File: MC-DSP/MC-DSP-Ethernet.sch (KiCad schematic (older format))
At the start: 29 parts

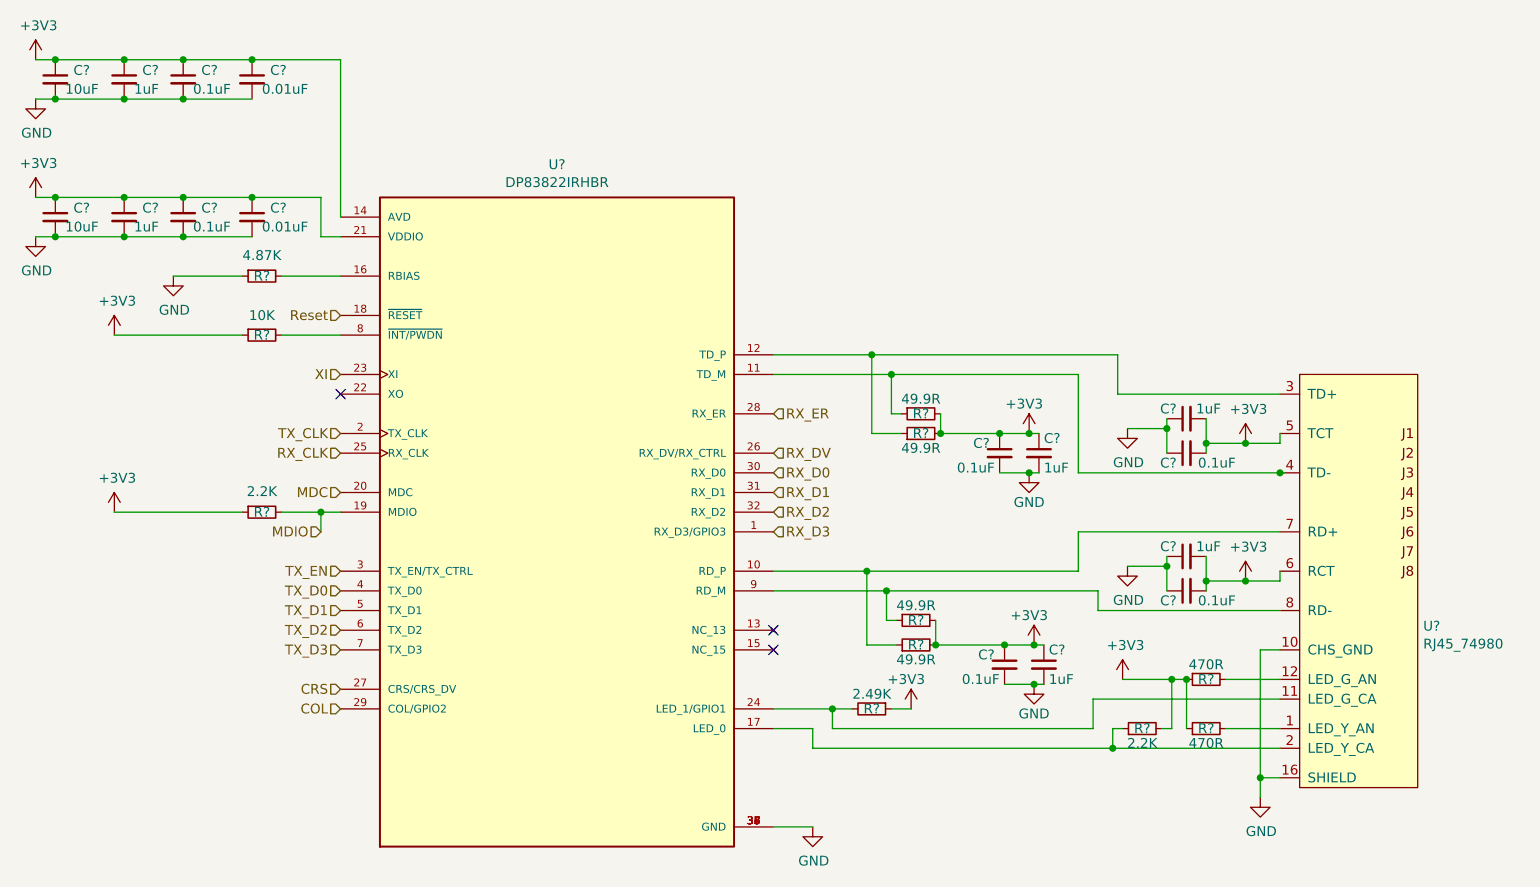
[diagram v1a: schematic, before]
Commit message: All parts labeled, just need to pick passives basically.
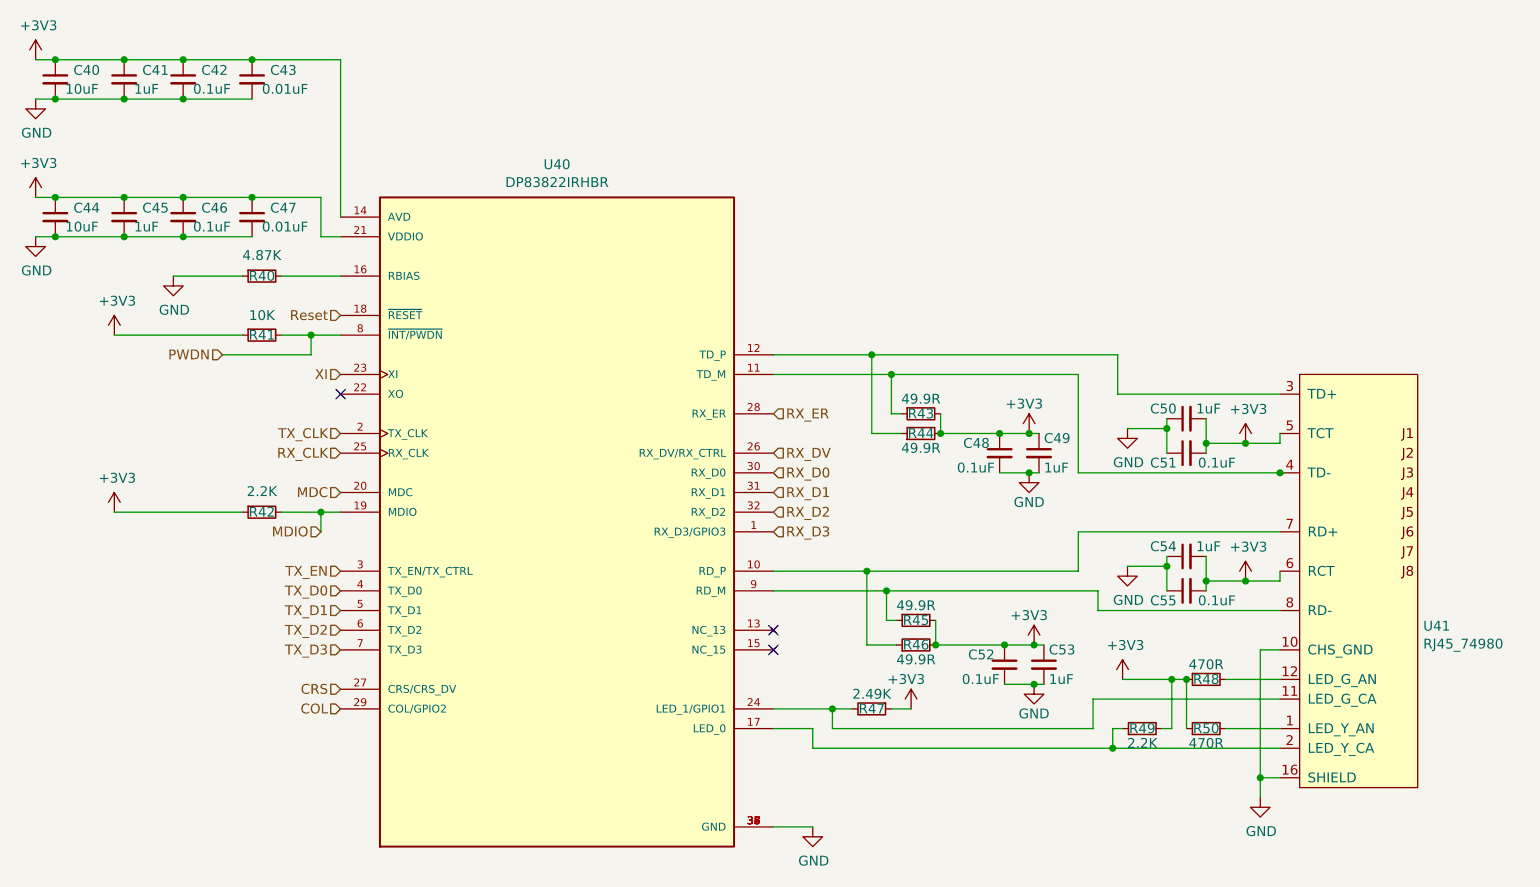
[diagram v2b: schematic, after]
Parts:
- C40, C41, C42, C43, C44, C45, C46, C47, C48, C49, C50, C51, C52, C53, C54, C55: renamed from C?; footprint (none) -> Capacitor_SMD:C_0201_0603Metric_Pad0.64x0.40mm_HandSolder
- R40, R41, R42, R43, R44, R45, R46, R47, R48, R49, R50: renamed from R?; footprint (none) -> Resistor_SMD:R_0603_1608Metric_Pad0.98x0.95mm_HandSolder
- gave numbers to parts that had none: 2
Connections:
- net PWDN: now reaches R41.2, U40.8 (~INT/PWDN)

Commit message: DSP - added footprints and links to most parts
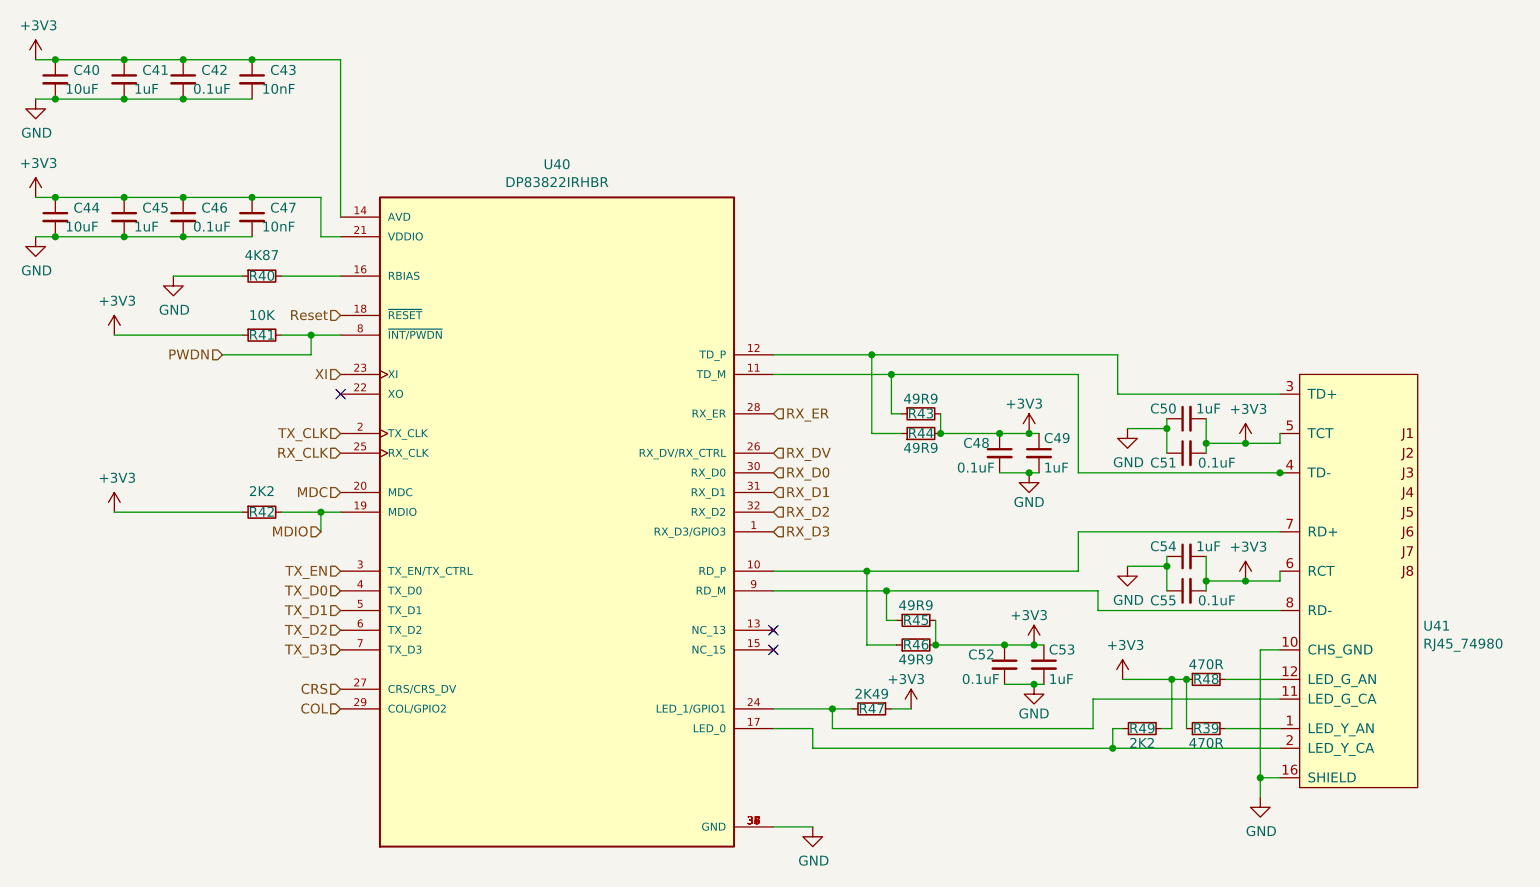
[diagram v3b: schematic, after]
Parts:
- C43, C47: value 0.01uF -> 10nF
- R40: value 4.87K -> 4K87
- R42, R49: value 2.2K -> 2K2
- R43, R44, R45, R46: value 49.9R -> 49R9
- R47: value 2.49K -> 2K49
- renumbered R50 to R39

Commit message: Removed clock buffer, misc leds, ethernet
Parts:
- C40, C41, C42, C43, C44, C45, C46, C47, C48, C49, C50, C51, C52, C53, C54, C55: footprint Capacitor_SMD:C_0201_0603Metric_Pad0.64x0.40mm_HandSolder -> Capacitor_SMD:C_0603_1608Metric_Pad1.08x0.95mm_HandSolder
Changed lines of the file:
@@
 F 0 "C44" H 1692 1896 50  0000 L CNN
 F 1 "10uF" H 1650 1800 50  0000 L CNN
-F 2 "Capacitor_SMD:C_0201_0603Metric_Pad0.64x0.40mm_HandSolder" H 1600 1850 50  0001 C CNN
+F 2 "Capacitor_SMD:C_0603_1608Metric_Pad1.08x0.95mm_HandSolder" H 1600 1850 50  0001 C CNN
 F 3 "https://www.digikey.com/en/products/detail/kemet/C0603C104K5RECAUTO/6575893?s=N4IgjCBcpgLFoDGUBmBDANgZwKYBoQB7KAbRACYBmADgHYaQBdAgBwBcoQBlNgJwEsAdgHMQAXwJgAbAhDJI6bPiKkQlAJzlYM5iHaceAkeIIBacrPl8ArsuKQyAVhAF1TCSFNvocqDbuqEIxiHhYO4AAM1gBiTAQyPvwAJpymYBEWrByQIC4gbACeLDicSVjIIUA" H 1600 1850 50  0001 C CNN
 	1    1600 1850
@@
 F 0 "C45" H 2042 1896 50  0000 L CNN
 F 1 "1uF" H 2000 1800 50  0000 L CNN
-F 2 "Capacitor_SMD:C_0201_0603Metric_Pad0.64x0.40mm_HandSolder" H 1950 1850 50  0001 C CNN
+F 2 "Capacitor_SMD:C_0603_1608Metric_Pad1.08x0.95mm_HandSolder" H 1950 1850 50  0001 C CNN
 F 3 "https://www.digikey.com/en/products/detail/yageo/CC0603KRX7R9BB104/2103082" H 1950 1850 50  0001 C CNN
 	1    1950 1850
@@
 F 0 "C46" H 2342 1896 50  0000 L CNN
 F 1 "0.1uF" H 2300 1800 50  0000 L CNN
-F 2 "Capacitor_SMD:C_0201_0603Metric_Pad0.64x0.40mm_HandSolder" H 2250 1850 50  0001 C CNN
+F 2 "Capacitor_SMD:C_0603_1608Metric_Pad1.08x0.95mm_HandSolder" H 2250 1850 50  0001 C CNN
 F 3 "https://www.digikey.com/en/products/detail/yageo/CC0603KRX7R9BB104/2103082" H 2250 1850 50  0001 C CNN
 	1    2250 1850
@@
 F 0 "C47" H 2692 1896 50  0000 L CNN
 F 1 "10nF" H 2650 1800 50  0000 L CNN
-F 2 "Capacitor_SMD:C_0201_0603Metric_Pad0.64x0.40mm_HandSolder" H 2600 1850 50  0001 C CNN
+F 2 "Capacitor_SMD:C_0603_1608Metric_Pad1.08x0.95mm_HandSolder" H 2600 1850 50  0001 C CNN
 F 3 "https://www.digikey.com/en/products/detail/kemet/C0603X103J4HAC7867/8334457" H 2600 1850 50  0001 C CNN
 	1    2600 1850
@@
 F 0 "C40" H 1692 1196 50  0000 L CNN
 F 1 "10uF" H 1650 1100 50  0000 L CNN
-F 2 "Capacitor_SMD:C_0201_0603Metric_Pad0.64x0.40mm_HandSolder" H 1600 1150 50  0001 C CNN
+F 2 "Capacitor_SMD:C_0603_1608Metric_Pad1.08x0.95mm_HandSolder" H 1600 1150 50  0001 C CNN
 F 3 "https://www.digikey.com/en/products/detail/kemet/C0603C104K5RECAUTO/6575893?s=N4IgjCBcpgLFoDGUBmBDANgZwKYBoQB7KAbRACYBmADgHYaQBdAgBwBcoQBlNgJwEsAdgHMQAXwJgAbAhDJI6bPiKkQlAJzlYM5iHaceAkeIIBacrPl8ArsuKQyAVhAF1TCSFNvocqDbuqEIxiHhYO4AAM1gBiTAQyPvwAJpymYBEWrByQIC4gbACeLDicSVjIIUA" H 1600 1150 50  0001 C CNN
 	1    1600 1150
@@
 F 0 "C41" H 2042 1196 50  0000 L CNN
 F 1 "1uF" H 2000 1100 50  0000 L CNN
-F 2 "Capacitor_SMD:C_0201_0603Metric_Pad0.64x0.40mm_HandSolder" H 1950 1150 50  0001 C CNN
+F 2 "Capacitor_SMD:C_0603_1608Metric_Pad1.08x0.95mm_HandSolder" H 1950 1150 50  0001 C CNN
 F 3 "https://www.digikey.com/en/products/detail/yageo/CC0603KRX7R9BB104/2103082" H 1950 1150 50  0001 C CNN
 	1    1950 1150
@@
 F 0 "C42" H 2342 1196 50  0000 L CNN
 F 1 "0.1uF" H 2300 1100 50  0000 L CNN
-F 2 "Capacitor_SMD:C_0201_0603Metric_Pad0.64x0.40mm_HandSolder" H 2250 1150 50  0001 C CNN
+F 2 "Capacitor_SMD:C_0603_1608Metric_Pad1.08x0.95mm_HandSolder" H 2250 1150 50  0001 C CNN
 F 3 "https://www.digikey.com/en/products/detail/yageo/CC0603KRX7R9BB104/2103082" H 2250 1150 50  0001 C CNN
 	1    2250 1150
@@
 F 0 "C43" H 2692 1196 50  0000 L CNN
 F 1 "10nF" H 2650 1100 50  0000 L CNN
-F 2 "Capacitor_SMD:C_0201_0603Metric_Pad0.64x0.40mm_HandSolder" H 2600 1150 50  0001 C CNN
+F 2 "Capacitor_SMD:C_0603_1608Metric_Pad1.08x0.95mm_HandSolder" H 2600 1150 50  0001 C CNN
 F 3 "https://www.digikey.com/en/products/detail/kemet/C0603X103J4HAC7867/8334457" H 2600 1150 50  0001 C CNN
 	1    2600 1150
@@
 F 0 "C52" H 6475 4175 50  0000 L CNN
 F 1 "0.1uF" H 6450 4050 50  0000 L CNN
-F 2 "Capacitor_SMD:C_0201_0603Metric_Pad0.64x0.40mm_HandSolder" H 6425 4125 50  0001 C CNN
+F 2 "Capacitor_SMD:C_0603_1608Metric_Pad1.08x0.95mm_HandSolder" H 6425 4125 50  0001 C CNN
 F 3 "https://www.digikey.com/en/products/detail/yageo/CC0603KRX7R9BB104/2103082" H 6425 4125 50  0001 C CNN
 	1    6425 4125
@@
 F 0 "C53" H 6650 4200 50  0000 L CNN
 F 1 "1uF" H 6650 4050 50  0000 L CNN
-F 2 "Capacitor_SMD:C_0201_0603Metric_Pad0.64x0.40mm_HandSolder" H 6625 4125 50  0001 C CNN
+F 2 "Capacitor_SMD:C_0603_1608Metric_Pad1.08x0.95mm_HandSolder" H 6625 4125 50  0001 C CNN
 F 3 "https://www.digikey.com/en/products/detail/yageo/CC0603KRX7R9BB104/2103082" H 6625 4125 50  0001 C CNN
 	1    6625 4125
@@
 F 0 "C48" H 6450 3100 50  0000 L CNN
 F 1 "0.1uF" H 6425 2975 50  0000 L CNN
-F 2 "Capacitor_SMD:C_0201_0603Metric_Pad0.64x0.40mm_HandSolder" H 6400 3050 50  0001 C CNN
+F 2 "Capacitor_SMD:C_0603_1608Metric_Pad1.08x0.95mm_HandSolder" H 6400 3050 50  0001 C CNN
 F 3 "https://www.digikey.com/en/products/detail/yageo/CC0603KRX7R9BB104/2103082" H 6400 3050 50  0001 C CNN
 	1    6400 3050
@@
 F 0 "C49" H 6625 3125 50  0000 L CNN
 F 1 "1uF" H 6625 2975 50  0000 L CNN
-F 2 "Capacitor_SMD:C_0201_0603Metric_Pad0.64x0.40mm_HandSolder" H 6600 3050 50  0001 C CNN
+F 2 "Capacitor_SMD:C_0603_1608Metric_Pad1.08x0.95mm_HandSolder" H 6600 3050 50  0001 C CNN
 F 3 "https://www.digikey.com/en/products/detail/yageo/CC0603KRX7R9BB104/2103082" H 6600 3050 50  0001 C CNN
 	1    6600 3050
@@
 F 0 "C55" V 7400 3800 50  0000 L CNN
 F 1 "0.1uF" V 7400 3500 50  0000 L CNN
-F 2 "Capacitor_SMD:C_0201_0603Metric_Pad0.64x0.40mm_HandSolder" H 7350 3750 50  0001 C CNN
+F 2 "Capacitor_SMD:C_0603_1608Metric_Pad1.08x0.95mm_HandSolder" H 7350 3750 50  0001 C CNN
 F 3 "https://www.digikey.com/en/products/detail/yageo/CC0603KRX7R9BB104/2103082" H 7350 3750 50  0001 C CNN
 	1    7350 3750
@@
 F 0 "C54" V 7400 3625 50  0000 L CNN
 F 1 "1uF" V 7400 3400 50  0000 L CNN
-F 2 "Capacitor_SMD:C_0201_0603Metric_Pad0.64x0.40mm_HandSolder" H 7350 3575 50  0001 C CNN
+F 2 "Capacitor_SMD:C_0603_1608Metric_Pad1.08x0.95mm_HandSolder" H 7350 3575 50  0001 C CNN
 F 3 "https://www.digikey.com/en/products/detail/yageo/CC0603KRX7R9BB104/2103082" H 7350 3575 50  0001 C CNN
 	1    7350 3575
@@
 F 0 "C51" V 7400 3100 50  0000 L CNN
 F 1 "0.1uF" V 7400 2800 50  0000 L CNN
-F 2 "Capacitor_SMD:C_0201_0603Metric_Pad0.64x0.40mm_HandSolder" H 7350 3050 50  0001 C CNN
+F 2 "Capacitor_SMD:C_0603_1608Metric_Pad1.08x0.95mm_HandSolder" H 7350 3050 50  0001 C CNN
 F 3 "https://www.digikey.com/en/products/detail/yageo/CC0603KRX7R9BB104/2103082" H 7350 3050 50  0001 C CNN
 	1    7350 3050
@@
 F 0 "C50" V 7400 2925 50  0000 L CNN
 F 1 "1uF" V 7400 2700 50  0000 L CNN
-F 2 "Capacitor_SMD:C_0201_0603Metric_Pad0.64x0.40mm_HandSolder" H 7350 2875 50  0001 C CNN
+F 2 "Capacitor_SMD:C_0603_1608Metric_Pad1.08x0.95mm_HandSolder" H 7350 2875 50  0001 C CNN
 F 3 "https://www.digikey.com/en/products/detail/yageo/CC0603KRX7R9BB104/2103082" H 7350 2875 50  0001 C CNN
 	1    7350 2875
